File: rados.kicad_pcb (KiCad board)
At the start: 2 copper layers, 83.5 x 106 mm, 158 parts, among them J1 HEADER, J10 STEPSTICK, J11 STEPSTICK, J12 STEPSTICK, J13 MICROSD_SLOT_TFP09-2-12B, J2 HEADER, J3 HEADER, J4 STEPSTICK, J5 STEPSTICK, J6 STEPSTICK, J7 HEADER, J8 HEADER, J9 HEADER, P1 CONN_01X02, P10 CONN_01X04, P11 CONN_01X04, P12 CONN_01X04, P13 EXT_SD, P14 LCD, P15 LIMIT_SWITCHES, P16 LIMIT_SWITCHES_V, P17 CONN_01X03, P18 CONN_01X03, P19 CONN_01X03, P2 CONN_01X02, P20 CONN_01X03, P21 THERMISTORS, P22 CONN_01X05, P23 CONN_01X02, P24 CONN_01X02, P3 CONN_01X02, P4 CONN_01X02, P5 HP_MOSFETS, P6 MP_MOSFETS, P7 CONN_02X04, P8 CONN_01X04, P9 CONN_01X04, Q1 2N7002P, Q10 2N7002P, Q11 2N7002P, Q12 BC846BPDW1, Q13 BC846BPDW1, Q14 SI2318CDS-T1-GE3, Q15 IRFB7545PbF, Q16 2N7002P, Q17 2N7002P, Q18 BC846BPDW1, Q19 BC846BPDW1, Q2 2N7002P, Q20 SI2318CDS-T1-GE3, Q21 IRFB7545PbF, Q3 2N7002P, Q4 BC846BPDW1, Q5 BC846BPDW1, Q6 BC846BPDW1, Q7 IRFB7545PbF, Q8 SI2318CDS-T1-GE3, Q9 IRFB7545PbF, SW1 RESET, U1 ST1S14PHR, U2 24LC256, U3 ESP-12E

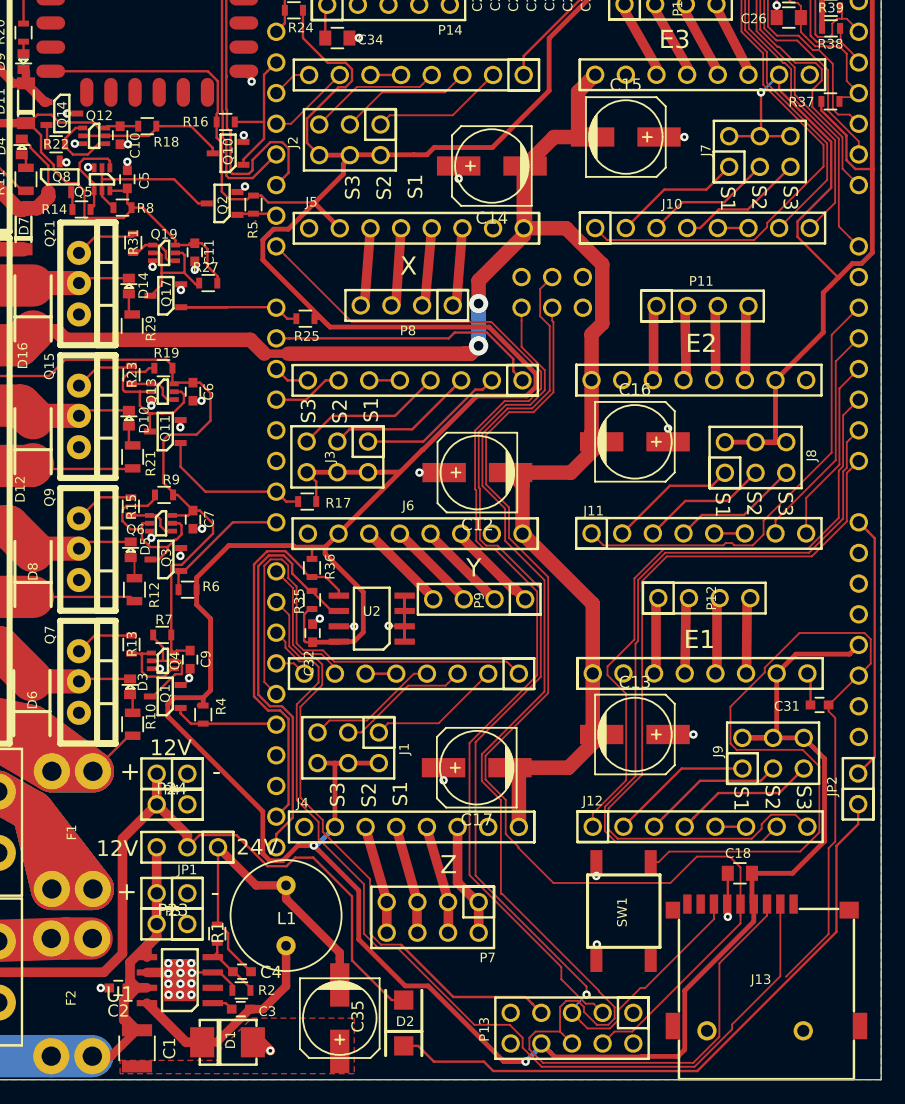
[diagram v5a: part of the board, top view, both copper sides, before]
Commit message: Silk placement
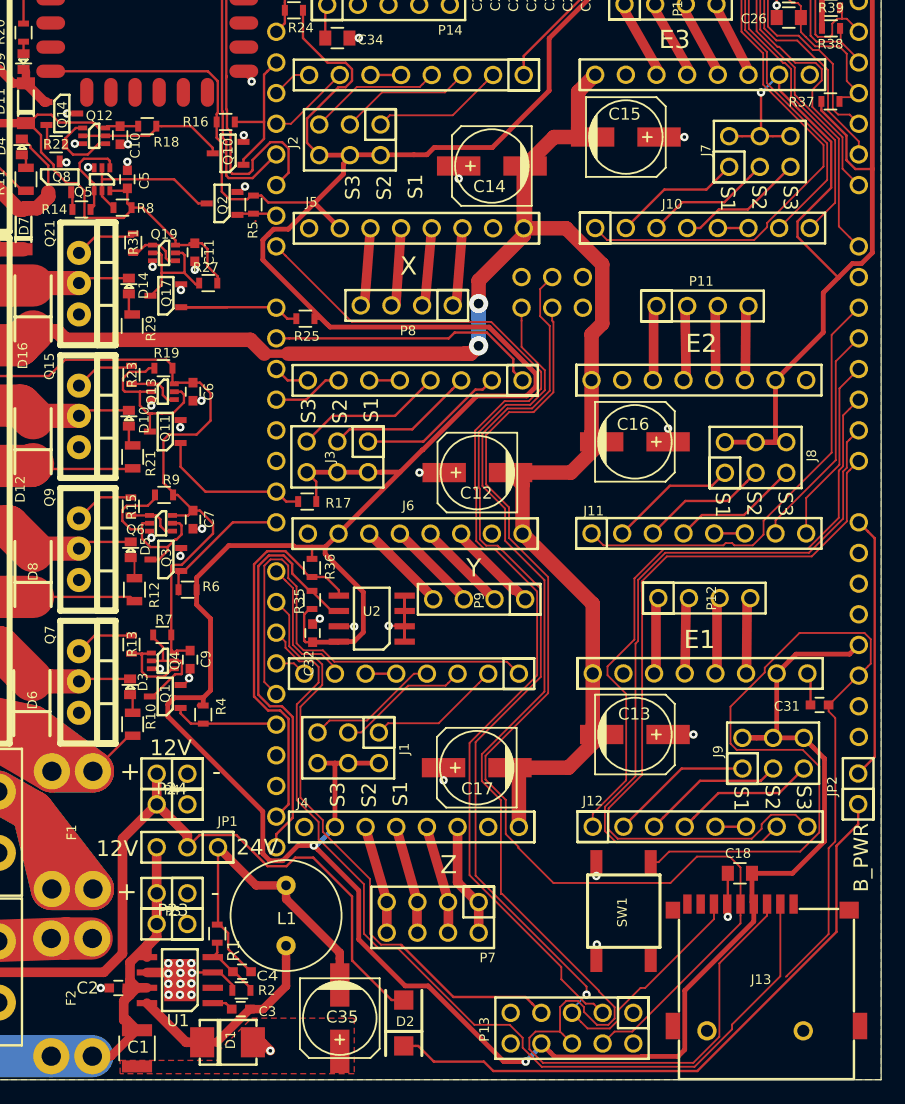
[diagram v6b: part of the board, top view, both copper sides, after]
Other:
- board text added: "B_PWR"
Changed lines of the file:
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@@
     (links 473)
     (no_connects 2)
-    (area 70.687299 23.987299 154.262701 130.012701)
+    (area 66.952441 19.858314 156.882162 159.290656)
     (thickness 1.6)
-    (drawings 35)
+    (drawings 36)
     (tracks 1891)
     (zones 0)
@@
   )
   (setup
-    (last_trace_width 0.2)
+    (last_trace_width 0.1524)
     (user_trace_width 0.1524)
     (user_trace_width 0.2)
@@
     (descr "SMT capacitor, aluminium electrolytic, 6.3x7.7")
     (attr smd)
-    (fp_text reference C12 (at 0 -4.318 180) (layer F.SilkS)
+    (fp_text reference C12 (at 0.1 -1.7 180) (layer F.SilkS)
       (effects (font (size 1 1) (thickness 0.15)))
     )
@@
     (descr Val)
     (attr smd)
-    (fp_text reference U1 (at 4.95 -1.2 180) (layer F.SilkS)
-      (effects (font (size 1.27 1.27) (thickness 0.1016)))
+    (fp_text reference U1 (at 0.15 -3.35 180) (layer F.SilkS)
+      (effects (font (size 1 1) (thickness 0.15)))
     )
     (fp_text value ST1S14PHR (at 0 0 180) (layer F.SilkS) hide
@@
     (at 96.774 110.744 270)
     (descr Val)
-    (fp_text reference JP1 (at 1.866 0.014 360) (layer F.SilkS)
+    (fp_text reference JP1 (at -2.144 -3.326 360) (layer F.SilkS)
       (effects (font (size 0.8 0.8) (thickness 0.15)))
     )
@@
     (descr "SMT capacitor, aluminium electrolytic, 6.3x7.7")
     (attr smd)
-    (fp_text reference C17 (at 0 -4.318 180) (layer F.SilkS)
+    (fp_text reference C17 (at -0.05 -1.75 180) (layer F.SilkS)
       (effects (font (size 1 1) (thickness 0.15)))
     )
@@
     (descr "SMT capacitor, aluminium electrolytic, 6.3x7.7")
     (attr smd)
-    (fp_text reference C16 (at 0 -4.318) (layer F.SilkS)
+    (fp_text reference C16 (at -0.15 -1.45) (layer F.SilkS)
       (effects (font (size 1 1) (thickness 0.15)))
     )
@@
     (descr "SMT capacitor, aluminium electrolytic, 6.3x7.7")
     (attr smd)
-    (fp_text reference C15 (at 0 -4.318) (layer F.SilkS)
+    (fp_text reference C15 (at -0.1 -1.9) (layer F.SilkS)
       (effects (font (size 1 1) (thickness 0.15)))
     )
@@
     (descr "SMT capacitor, aluminium electrolytic, 6.3x7.7")
     (attr smd)
-    (fp_text reference C14 (at 0 -4.318 180) (layer F.SilkS)
+    (fp_text reference C14 (at 0.2 -1.7 180) (layer F.SilkS)
       (effects (font (size 1 1) (thickness 0.15)))
     )
@@
     (descr "SMT capacitor, aluminium electrolytic, 6.3x7.7")
     (attr smd)
-    (fp_text reference C13 (at 0 -4.318) (layer F.SilkS)
+    (fp_text reference C13 (at -0.05082 -1.7) (layer F.SilkS)
       (effects (font (size 1 1) (thickness 0.15)))
     )
@@
     (tags "resistor 0603")
     (attr smd)
-    (fp_text reference R1 (at -0.1 -0.05 270) (layer F.SilkS)
+    (fp_text reference R1 (at 1.4 -1.35 270) (layer F.SilkS)
       (effects (font (size 1 1) (thickness 0.15)))
     )
@@
     (descr "SMT capacitor, aluminium electrolytic, 6.3x7.7")
     (attr smd)
-    (fp_text reference C35 (at -0.15 -1.5 270) (layer F.SilkS)
+    (fp_text reference C35 (at -0.1 -0.2 360) (layer F.SilkS)
       (effects (font (size 1 1) (thickness 0.15)))
     )
@@
     (tags "capacitor 1210")
     (attr smd)
-    (fp_text reference C1 (at 0 -2.7 270) (layer F.SilkS)
+    (fp_text reference C1 (at -0.1 -0.1 360) (layer F.SilkS)
       (effects (font (size 1 1) (thickness 0.15)))
     )
@@
     (tags "capacitor 0603")
     (attr smd)
-    (fp_text reference C4 (at -2.4 -0.05 180) (layer F.SilkS)
-      (effects (font (size 1 1) (thickness 0.15)))
+    (fp_text reference C4 (at -2.1 -0.35 180) (layer F.SilkS)
+      (effects (font (size 0.8 1) (thickness 0.15)))
     )
     (fp_text value DNP (at 0 1.9 180) (layer F.Fab)
@@
     (tags "capacitor 0603")
     (attr smd)
-    (fp_text reference C2 (at 0 -1.9 180) (layer F.SilkS)
+    (fp_text reference C2 (at 2.55 0 180) (layer F.SilkS)
       (effects (font (size 1 1) (thickness 0.15)))
     )
@@
     )
   )
+  (gr_text B_PWR (at 152.6 111.6 90) (layer F.SilkS)
+    (effects (font (size 1.2 1.2) (thickness 0.2)))
+  )
   (gr_text E3 (at 137.14 43.83) (layer F.SilkS)

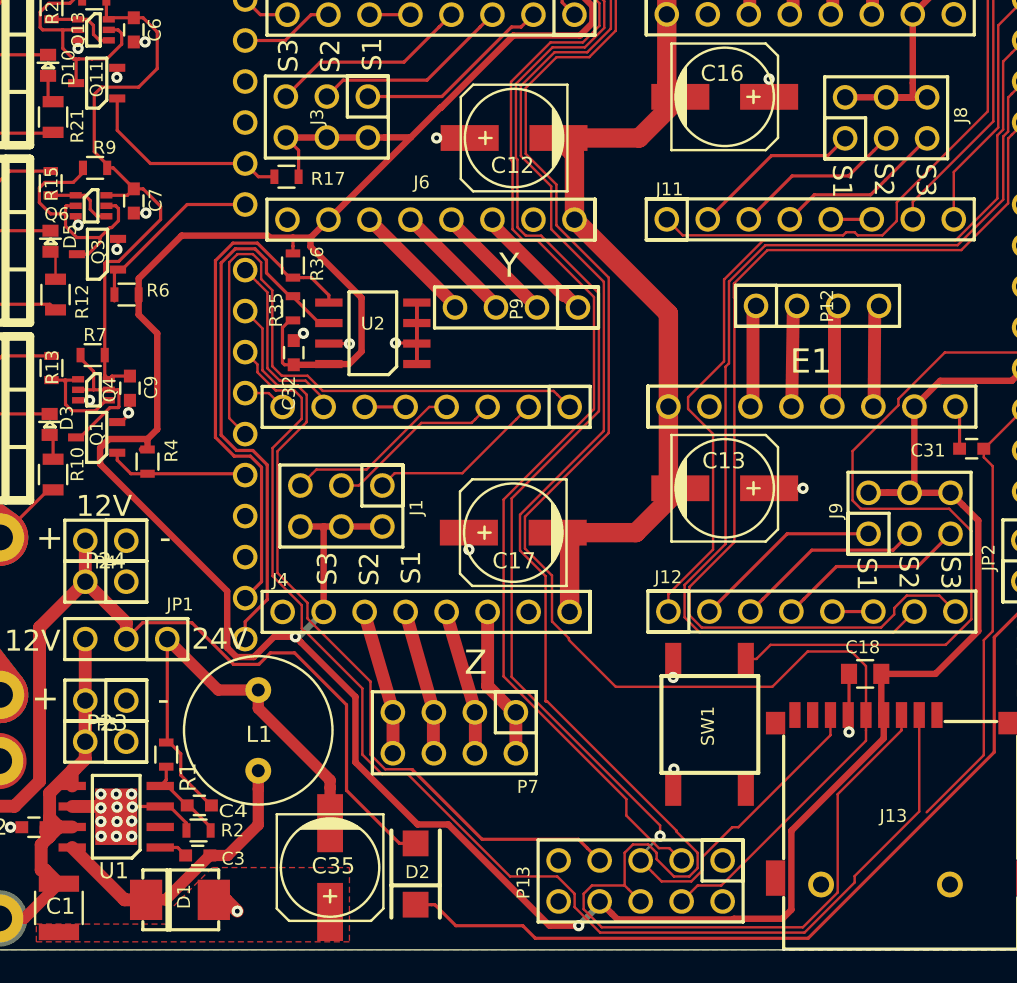
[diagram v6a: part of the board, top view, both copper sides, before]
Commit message: Moved heatbed io away from arduino led-output (D13)
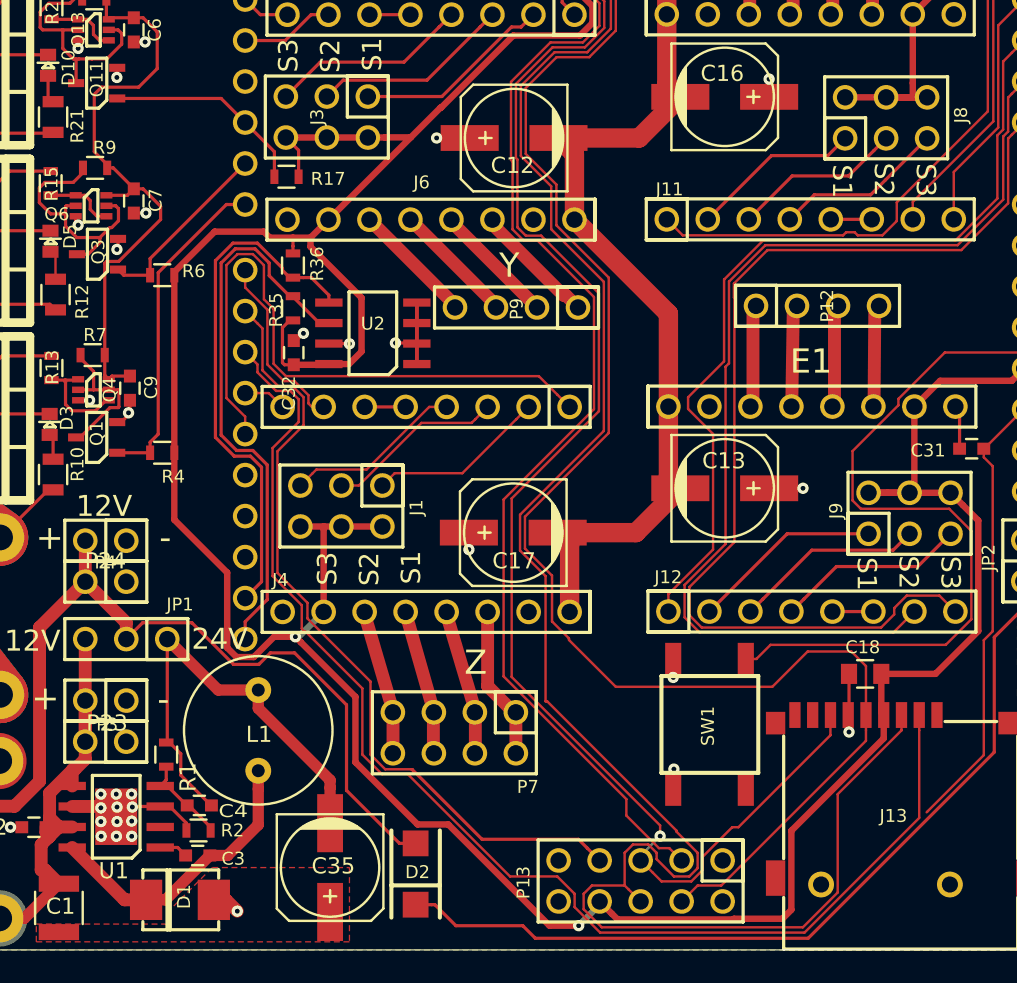
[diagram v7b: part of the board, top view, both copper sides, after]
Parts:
- moved R6 2.51 mm to (99.0, 88.2)
- moved R4 1.06 mm to (99.0, 99.2), turned to 0 degrees
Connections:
- SHIELD1 pad 13: HB-FET -> Net-(SHIELD1-Pad13)
- SHIELD1 pad 5: Net-(SHIELD1-Pad5) -> HP-FET2
- SHIELD1 pad 6: HP-FET2 -> HP-FET1
- SHIELD1 pad 7: HP-FET1 -> HB-FET
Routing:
- net HB-FET: track 8.88 -> 21.0 mm
- net +3V3: track 566.1 -> 557.9 mm
- net HP-FET1: track 12.0 -> 11.5 mm

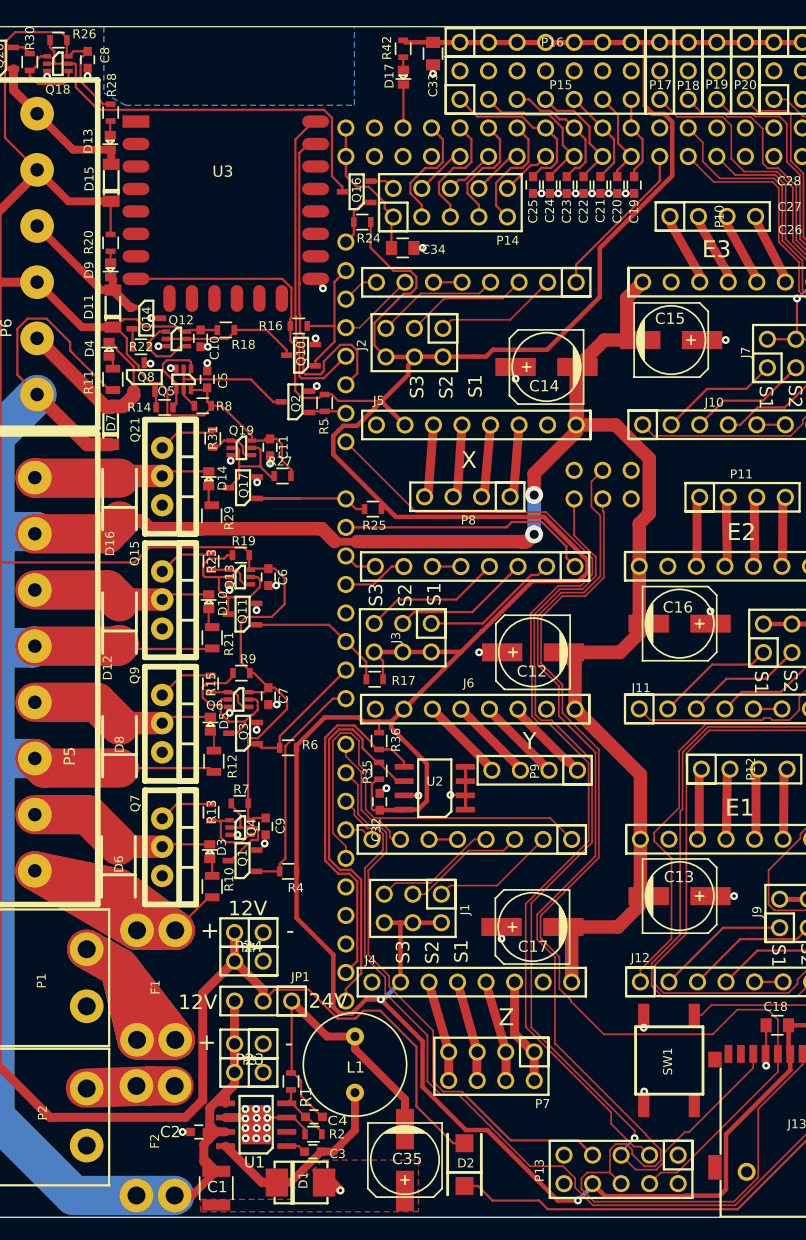
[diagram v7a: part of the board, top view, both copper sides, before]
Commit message: - Some mosfets now can have hardware PWM - moved eeprom to i2c with arduino pull-ups
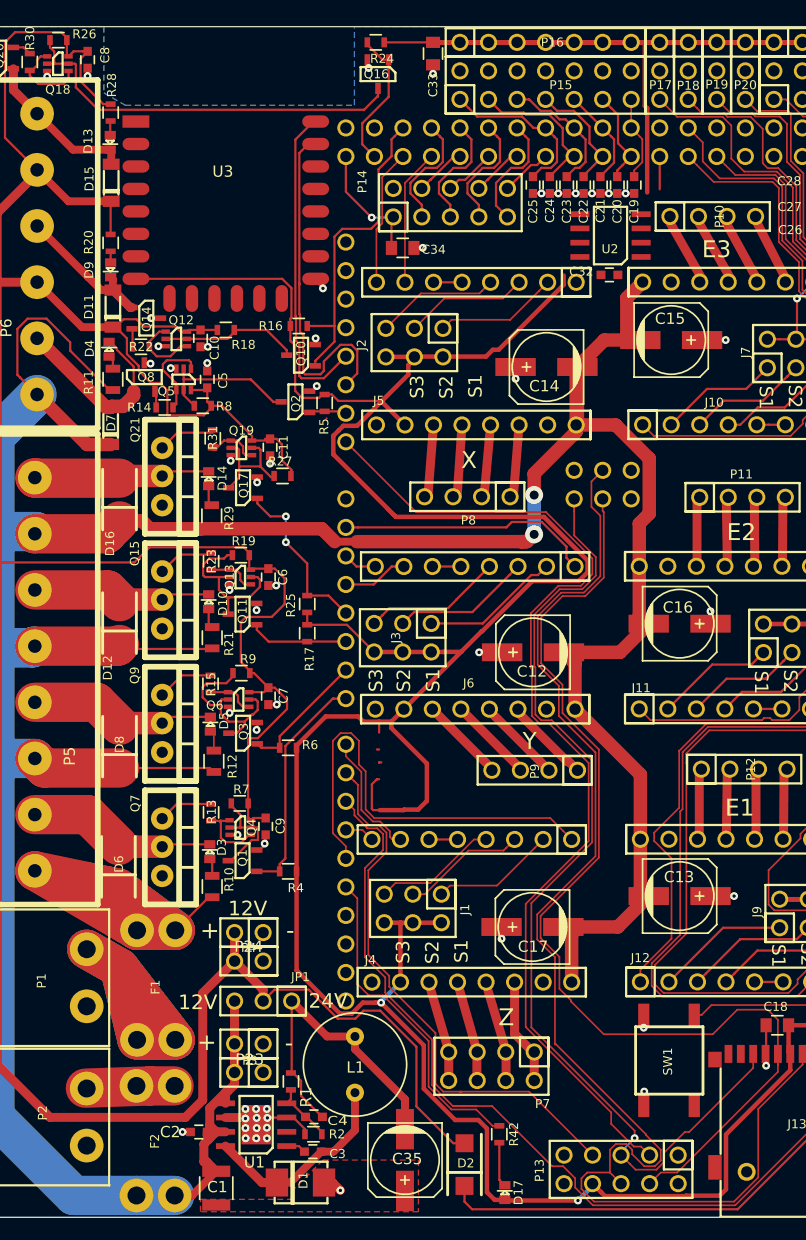
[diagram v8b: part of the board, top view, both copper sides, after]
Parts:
- removed R35, R36: 4K7, resistors:R_0603
- R42: value 470R -> 1K
- moved D17 99.7 mm to (118.3, 127.8), turned to 90 degrees
- moved R42 97.0 mm to (117.8, 122.6), turned to 90 degrees
- moved U2 51.6 mm to (127.7, 42.6)
- moved C32 51.2 mm to (127.6, 46.1), turned to 0 degrees
- moved R24 16.0 mm to (106.8, 25.4)
- moved Q16 10.6 mm to (107.0, 28.2), turned to 270 degrees
- moved R25 10.3 mm to (100.7, 75.4), turned to 270 degrees
- moved R17 7.27 mm to (100.7, 78.0), turned to 90 degrees
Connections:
- D17 pad 1: Net-(D17-Pad1) -> +3V3
- D17 pad 2: STATUS-LED -> Net-(D17-Pad2)
- R42 pad 1: +3V3 -> Net-(D17-Pad2)
- R42 pad 2: Net-(D17-Pad1) -> STATUS-LED
- SHIELD1 pad 0: HP-FET3 -> Net-(SHIELD1-Pad0)
- SHIELD1 pad 13: Net-(SHIELD1-Pad13) -> STATUS-LED
- SHIELD1 pad 18: X-STEP -> Net-(SHIELD1-Pad18)
- SHIELD1 pad 19: X-DIR -> Net-(SHIELD1-Pad19)
- SHIELD1 pad 20: LP-FET1 -> SDA1
- SHIELD1 pad 21: LP-FET2 -> SCL1
- SHIELD1 pad 22: Net-(SHIELD1-Pad22) -> LP-FET2
- SHIELD1 pad 24: Net-(SHIELD1-Pad24) -> X-DIR
- SHIELD1 pad 25: STATUS-LED -> LP-FET1
- SHIELD1 pad 26: Net-(SHIELD1-Pad26) -> X-STEP
- SHIELD1 pad 4: CS1 -> HP-FET3
- SHIELD1 pad SCL1: SCL1 -> Net-(SHIELD1-PadSCL1)
- SHIELD1 pad SDA1: SDA1 -> Net-(SHIELD1-PadSDA1)
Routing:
- net SCL1: track 35.1 -> 0.00 mm
- net SDA1: track 32.4 -> 0.24 mm
- net STATUS-LED: track 3.88 -> 29.4 mm
- net +3V3: track 557.9 -> 535.2 mm
- net LP-FET1: track 12.3 -> 28.4 mm
- net GND: track 94.3 -> 81.8 mm, vias 60 -> 58
- net X-EN: track 14.3 -> 2.93 mm
- net X-DIR: track 3.34 -> 12.4 mm
- net LP-FET2: track 4.87 -> 12.7 mm
- net X-STEP: track 6.93 -> 12.6 mm
- net Net-(D17-Pad2): track 0.00 -> 4.26 mm
- net HP-FET2: track 12.7 -> 8.82 mm
- net Net-(Q16-Pad3): track 37.7 -> 35.8 mm
- net SD-CS: track 78.7 -> 80.7 mm
- net +5V: track 13.1 -> 11.2 mm, vias 0 -> 1
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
